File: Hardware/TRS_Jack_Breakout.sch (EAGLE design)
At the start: 4 parts

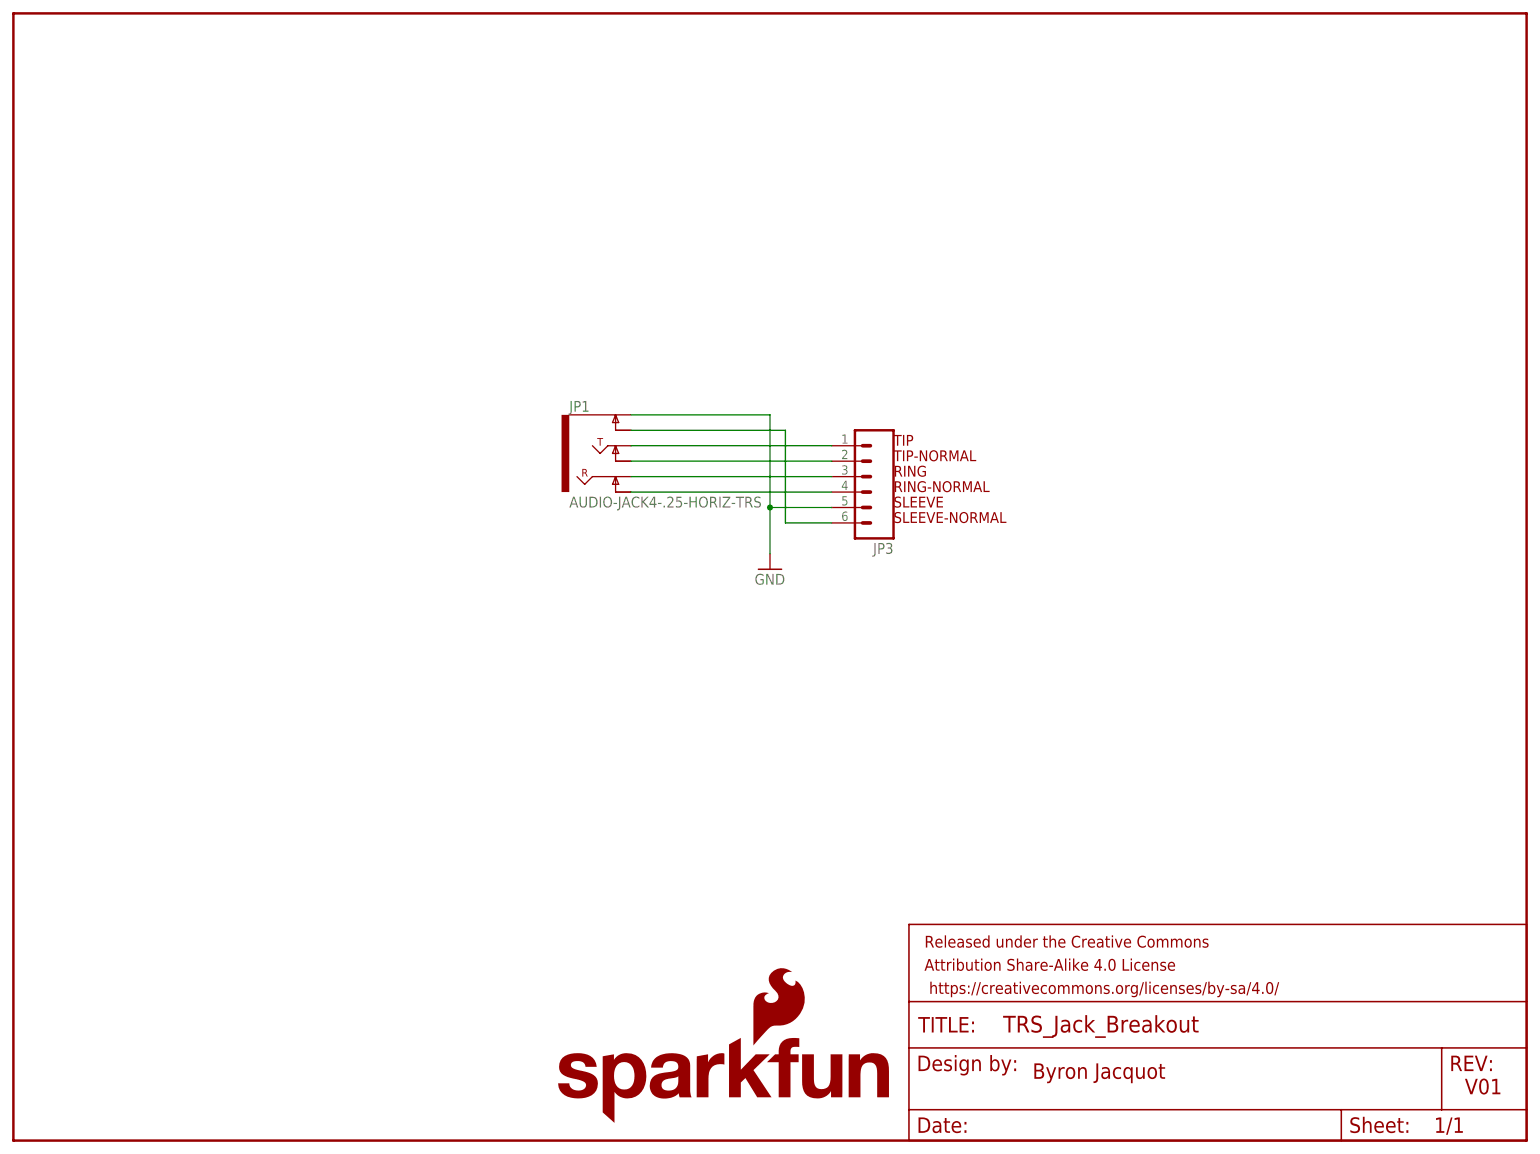
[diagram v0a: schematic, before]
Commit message: Adding mounting holes on tabls, gnd pin
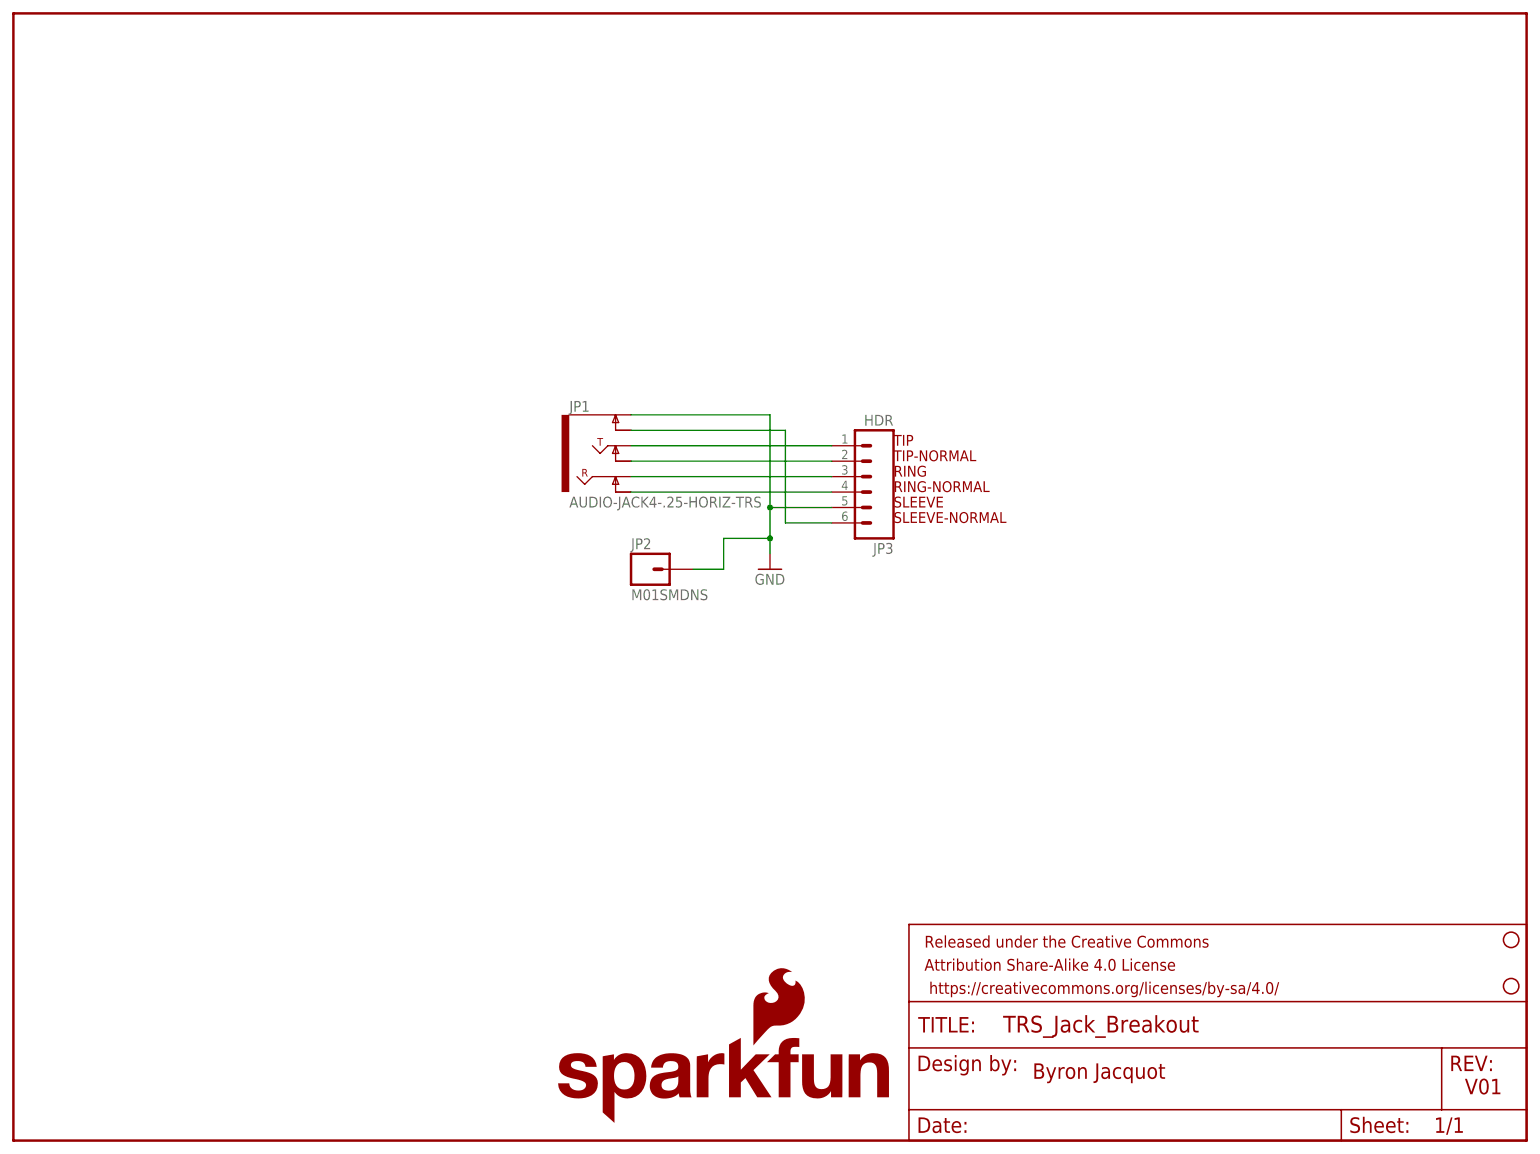
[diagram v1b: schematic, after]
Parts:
- added JP2: M01SMDNS, SparkFun-Connectors:M01SMDNS
- added STANDOFF1, STANDOFF2: STAND-OFF, SparkFun-Electromechanical:STAND-OFF
- JP3: value (none) -> HDR
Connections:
- net GND: now also JP2.1
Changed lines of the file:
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@@
 <part name="FRAME1" library="SparkFun-Aesthetics" deviceset="FRAME-LETTER" device=""/>
 <part name="JP1" library="SparkFun-Connectors" deviceset="AUDIO-JACK4-.25-HORIZ-TRS" device=""/>
-<part name="JP3" library="SparkFun-Connectors" deviceset="M06" device="NO_SILK"/>
+<part name="JP3" library="SparkFun-Connectors" deviceset="M06" device="NO_SILK" value="HDR"/>
 <part name="GND1" library="SparkFun-Aesthetics" deviceset="GND" device=""/>
 <part name="LOGO1" library="SparkFun-Aesthetics" deviceset="SFE_LOGO_NAME_FLAME" device=".1_INCH"/>
+<part name="STANDOFF1" library="SparkFun-Electromechanical" deviceset="STAND-OFF" device=""/>
+<part name="STANDOFF2" library="SparkFun-Electromechanical" deviceset="STAND-OFF" device=""/>
+<part name="JP2" library="SparkFun-Connectors" deviceset="M01" device="SMDNS"/>
 </parts>
 <sheets>
@@
 <instance part="GND1" gate="1" x="124.46" y="93.98"/>
 <instance part="LOGO1" gate="G$1" x="88.9" y="2.54"/>
+<instance part="STANDOFF1" gate="G$1" x="246.38" y="33.02"/>
+<instance part="STANDOFF2" gate="G$1" x="246.38" y="25.4"/>
+<instance part="JP2" gate="G$1" x="104.14" y="93.98"/>
 </instances>
 <busses>
@@
 <wire x1="124.46" y1="104.14" x2="134.62" y2="104.14" width="0.1524" layer="91"/>
 <pinref part="GND1" gate="1" pin="GND"/>
-<wire x1="124.46" y1="96.52" x2="124.46" y2="104.14" width="0.1524" layer="91"/>
+<wire x1="124.46" y1="96.52" x2="124.46" y2="99.06" width="0.1524" layer="91"/>
 <junction x="124.46" y="104.14"/>
+<wire x1="124.46" y1="99.06" x2="124.46" y2="104.14" width="0.1524" layer="91"/>
+<wire x1="111.76" y1="93.98" x2="116.84" y2="93.98" width="0.1524" layer="91"/>
+<wire x1="116.84" y1="93.98" x2="116.84" y2="99.06" width="0.1524" layer="91"/>
+<wire x1="116.84" y1="99.06" x2="124.46" y2="99.06" width="0.1524" layer="91"/>
+<junction x="124.46" y="99.06"/>
+<pinref part="JP2" gate="G$1" pin="1"/>
 </segment>
 </net>

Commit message: Updating footprint based on protos
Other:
- note added: "V10"
- note removed: "V01"
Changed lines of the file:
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@@
 <plain>
 <text x="167.64" y="10.16" size="2.54" layer="94">Byron Jacquot</text>
-<text x="238.76" y="7.62" size="2.54" layer="94">V01</text>
+<text x="238.76" y="7.62" size="2.54" layer="94">V10</text>
 <text x="144.78" y="114.3" size="1.778" layer="94">TIP</text>
 <text x="144.78" y="111.76" size="1.778" layer="94">TIP-NORMAL</text>
